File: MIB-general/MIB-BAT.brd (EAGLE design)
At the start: 70.8 x 49.5 mm, 19 parts, among them IC1 74LS14N, X1 MAB5SH, X2 MAB5SH

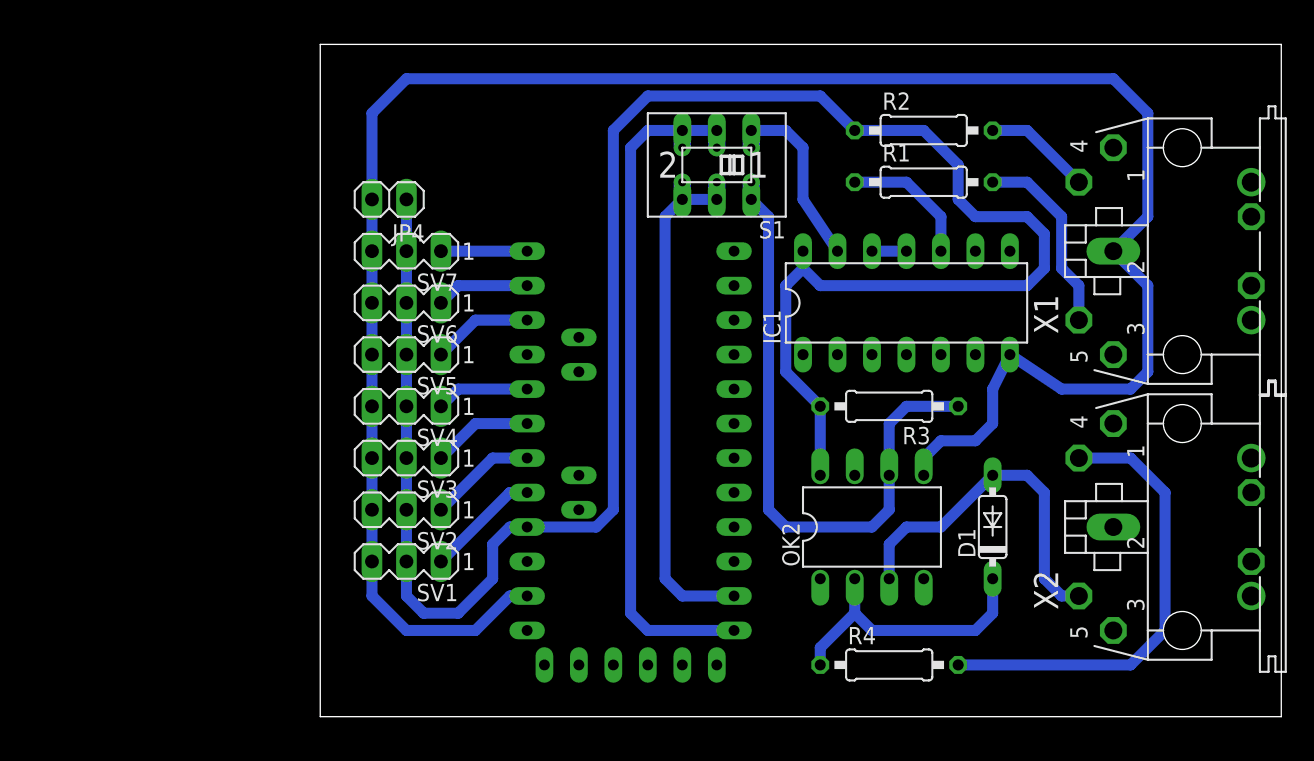
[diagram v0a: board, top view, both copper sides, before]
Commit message: Better version board with optional battery power supply
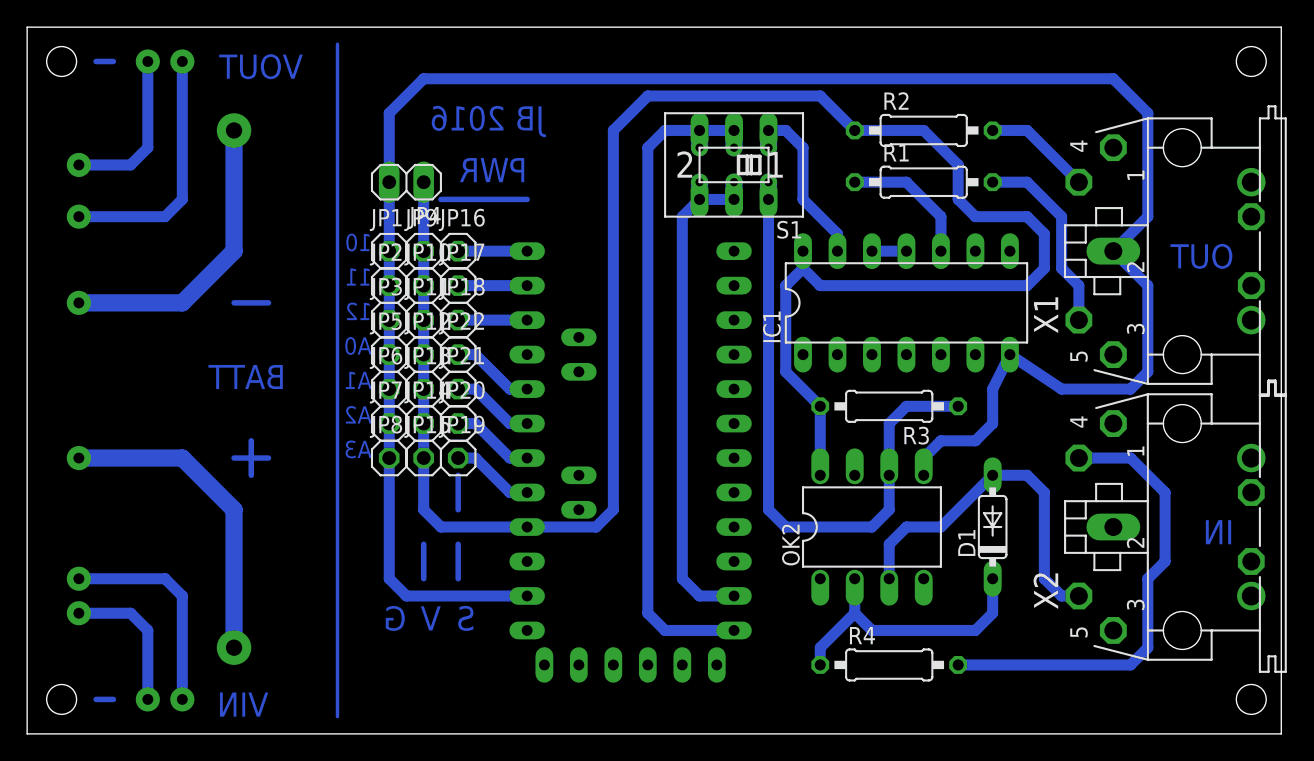
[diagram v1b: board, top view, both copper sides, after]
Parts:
- removed SV1, SV2, SV3, SV4, SV5, SV6, SV7: (no value), con-lstb:MA03-1
- added JP1, JP10, JP11, JP12, JP13, JP14, JP15, JP16, JP17, JP18, JP19, JP2, JP20, JP21, JP22, JP3, JP5, JP6, JP7, JP8, JP9: (no value), pinhead:1X01
- moved JP4 1.80 mm to (35.6, 69.8)
- moved S1 1.27 mm to (59.7, 71.1)
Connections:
- removed net N$9: IC1.14, JP4.1, OK2.8, R2.1, R3.2, SV1.2, SV2.2, SV3.2, SV4.2, SV5.2, SV6.2, SV7.2, U$1.VCC
- new net N$29: JP21.1, U$1.A2
- net N$11: now also JP1.1, JP2.1, JP3.1, JP5.1, JP6.1, JP7.1, JP8.1; no longer SV1.3, SV2.3, SV3.3, SV4.3, SV5.3, SV6.3, SV7.3
- net N$13: now also JP16.1, U$1.D10; no longer SV2.1, U$1.A1
- net N$14: now also JP17.1, U$1.D11; no longer SV3.1, U$1.A2
- net N$15: now also IC1.14, JP10.1, JP11.1, JP12.1, JP13.1, JP14.1, JP15.1, JP4.1, JP9.1, OK2.8, R2.1, R3.2, U$1.VCC; no longer SV4.1, U$1.A3
- net N$16: now also JP18.1, U$1.D12; no longer SV1.1, U$1.A0
- net N$18: now also JP19.1, U$1.A0; no longer SV5.1, U$1.D12
- net N$19: now also JP20.1, U$1.A1; no longer SV6.1, U$1.D11
- net N$30: now also JP22.1, U$1.A3; no longer SV7.1, U$1.D10
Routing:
- net N$9: track 155.5 -> 2.54 mm
- net N$15: track 6.88 -> 143.8 mm
- net N$40: track 0.00 -> 49.5 mm
- net N$25: track 0.00 -> 23.2 mm, vias 0 -> 2
- net N$24: track 0.00 -> 21.9 mm, vias 0 -> 2
- net N$27: track 0.00 -> 18.3 mm, vias 0 -> 2
- net N$33: track 0.00 -> 15.8 mm, vias 0 -> 2
- net N$26: track 0.00 -> 12.0 mm, vias 0 -> 2
- net N$34: track 0.00 -> 10.7 mm, vias 0 -> 2
- net N$39: track 0.00 -> 6.35 mm
- net N$29: track 0.00 -> 6.13 mm
- net N$11: track 153.7 -> 148.4 mm
- net N$16: track 8.45 -> 5.08 mm
- net N$13: track 7.93 -> 5.08 mm
- net N$38: track 0.00 -> 2.54 mm
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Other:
- board size 70.8 x 49.5 mm -> 92.4 x 52.1 mm
- board text added: "10"
- board text added: "11"
- board text added: "12"
- board text added: "A0"
- board text added: "A1"
- board text added: "A2"
- board text added: "A3"
- board text added: "BATT"
- board text added: "G"
- board text added: "IN"
- board text added: "JB 2016"
- board text added: "OUT"
- board text added: "PWR"
- board text added: "S"
- board text added: "V"
- board text added: "VIN"
- board text added: "VOUT"

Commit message: New PCB layout enabling choice of optocoupler and makes the buffer optional.
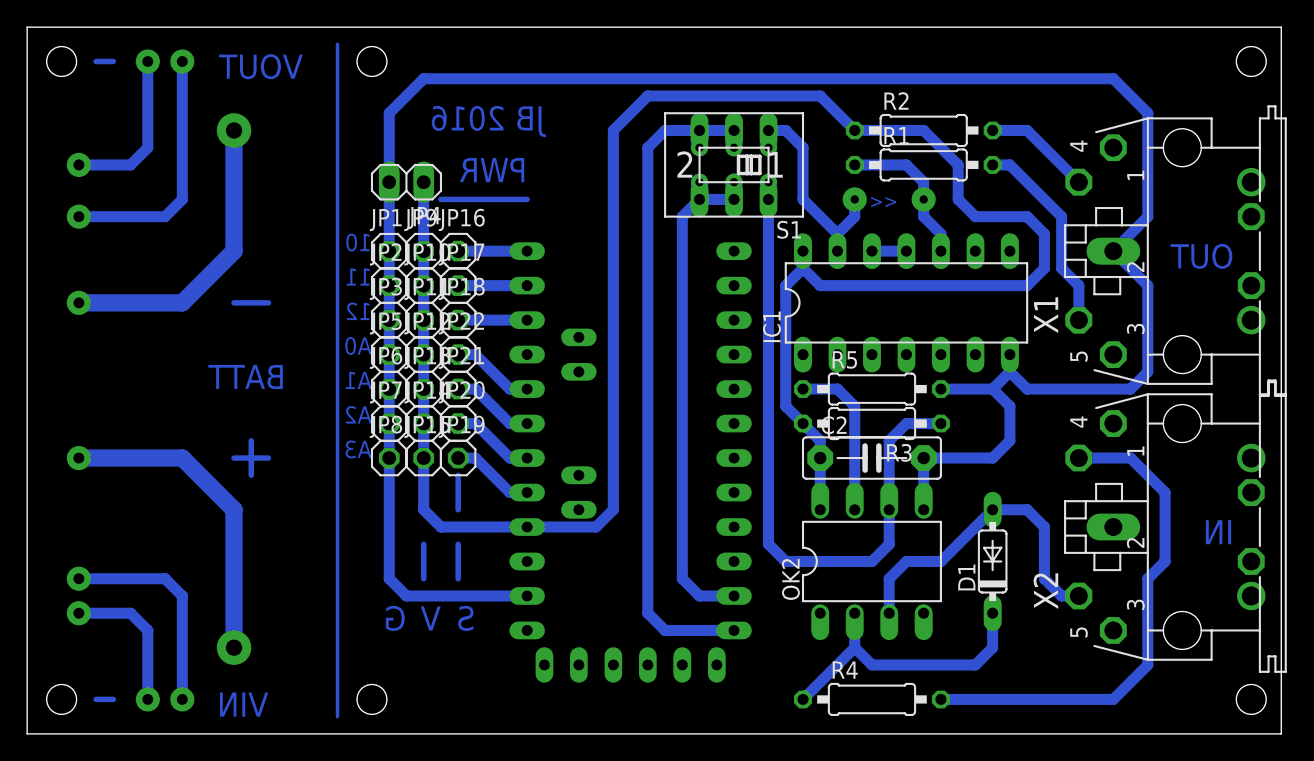
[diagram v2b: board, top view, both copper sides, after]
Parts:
- added C2: (no value), capacitor-wima:C7.5B3
- added R5: 2K2, rcl:0207/10
- R3: value 10K -> 2K2
- moved R4 2.84 mm to (69.8, 31.8)
- moved D1 2.54 mm to (78.7, 41.9)
- moved OK2 2.54 mm to (69.8, 41.9)
- moved R3 1.80 mm to (69.8, 52.1)
- moved R1 1.27 mm to (73.7, 71.1)
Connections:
- new net N$41: OK2.7, R5.1
- net N$11: now also C2.2, R5.2
- net N$15: now also C2.1
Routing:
- net N$41: track 0.00 -> 12.0 mm
- net N$11: track 148.4 -> 157.2 mm
- net N$5: track 33.9 -> 36.9 mm
- net N$42: track 13.0 -> 16.1 mm, vias 1 -> 2
- net N$15: track 143.8 -> 146.3 mm
- net N$10: track 46.0 -> 48.6 mm
- net N$6: track 26.0 -> 23.5 mm
- net N$3: track 9.94 -> 11.2 mm
- net N$7: track 14.3 -> 14.8 mm
- net N$4: track 21.2 -> 21.7 mm
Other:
- board text added: "<<"
- board text added: ">137"
- board text added: ">>"
